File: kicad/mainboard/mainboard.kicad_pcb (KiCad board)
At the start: 2 copper layers, 190.5 x 66 mm, 146 parts, among them J1 +12V BATTERY, J10 Conn 1x4, J12 Conn 02x03, J13 Conn_02x12, J2 REMOTE INPUT, J3 RADIO INTERFACE, J4 MIC INPUT, J5 LINE INPUT, J6 OUTPUT A, J7 OUTPUT B, J8 VDC INPUT, J9 LINK INPUT, T1 IRL520N, T2 IRL520N, T3 IRF9Z24, T4 IRL520N, T5 IRL520N, T6 IRF9Z24, U1 ATMEGA16/32-P, U10 LM358N, U11 7809TV, U12 7809TV, U13 7805TV, U2 LM324N, U4 LM358N, U5 LM2941T, U7 LTC1661, U8 MAX548A, U9 MAX232

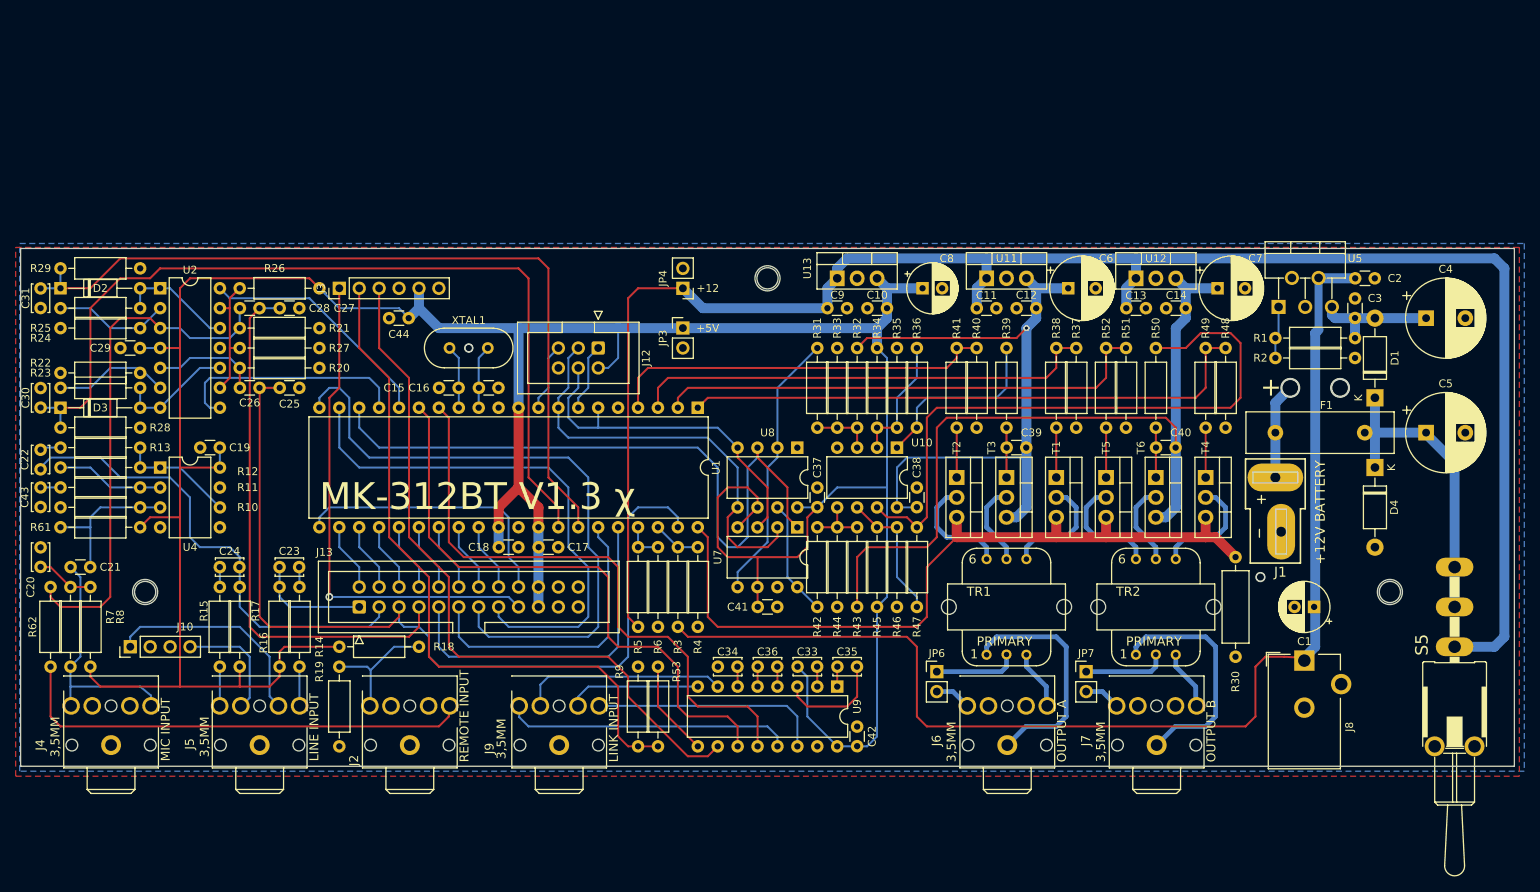
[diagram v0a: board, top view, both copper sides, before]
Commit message: Tiny fixups on mainboard: mounting holes and one audio jack
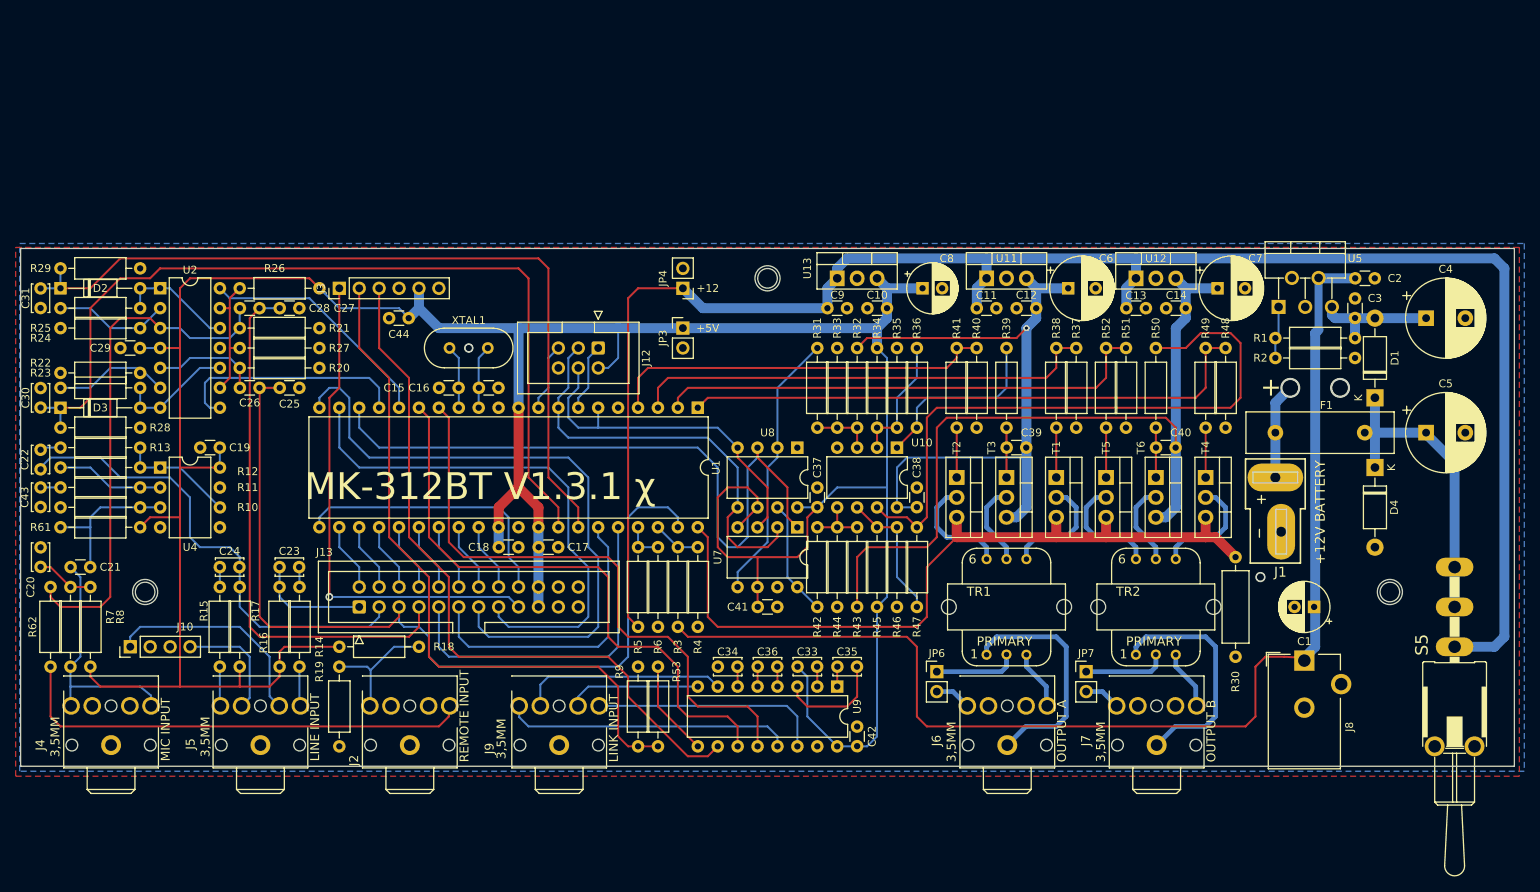
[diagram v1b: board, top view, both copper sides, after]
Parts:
- H1, H2, H3: footprint MountingHole:MountingHole_2.7mm_M2.5 -> MountingHole:MountingHole_2.5mm
- moved J5 0.10 mm to (81.3, 116.8)
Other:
- board text added: "MK-312BT V1.3.1 χ"
- board text removed: "MK-312BT V1.3 χ"
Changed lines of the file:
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@@
   )
   (paper "A4")
+  (title_block
+    (title "MK312-BT Mainboard")
+    (date "2022-08-01")
+    (rev "1.3.1-Chi")
+  )
   (layers
     (0 "F.Cu" signal)
@@
       (layerselection 0x00010fc_ffffffff)
       (disableapertmacros false)
-      (usegerberextensions false)
+      (usegerberextensions true)
       (usegerberattributes true)
       (usegerberadvancedattributes true)
-      (creategerberjobfile true)
+      (creategerberjobfile false)
       (svguseinch false)
       (svgprecision 6)
@@
       (outputformat 1)
       (mirror false)
-      (drillshape 1)
+      (drillshape 0)
       (scaleselection 1)
-      (outputdirectory "")
+      (outputdirectory "gerber")
     )
   )
@@
   )
   (footprint "mk312:STX3100" (layer "F.Cu")
-    (at 81.18 116.84 90)
+    (at 81.28 116.84 90)
     (descr "<b>MIC/HEADPHONE JACK</b><p>\nKS-S stereo microphone/headphone jack<p>\n PG203JN (Schukat)")
     (property "Sheetfile" "Input_stage.kicad_sch")
@@
     )
   )
-  (footprint "MountingHole:MountingHole_2.7mm_M2.5" (layer "F.Cu")
+  (footprint "MountingHole:MountingHole_2.5mm" (layer "F.Cu")
     (at 66.675 94.615)
-    (descr "Mounting Hole 2.7mm, no annular, M2.5")
-    (tags "mounting hole 2.7mm no annular m2.5")
+    (descr "Mounting Hole 2.5mm, no annular")
+    (tags "mounting hole 2.5mm no annular")
     (property "Sheetfile" "mainboard.kicad_sch")
     (property "Sheetname" "")
     (attr exclude_from_pos_files)
-    (fp_text reference "H3" (at 0 -3.7) (layer "F.SilkS") hide
+    (fp_text reference "H3" (at 0 -3.5) (layer "F.SilkS") hide
       (effects (font (size 1 1) (thickness 0.15)))
     )
-    (fp_text value "MountingHole" (at 0 3.7) (layer "F.Fab")
+    (fp_text value "MountingHole" (at 0 3.5) (layer "F.Fab")
       (effects (font (size 1 1) (thickness 0.15)))
     )
@@
       (effects (font (size 1 1) (thickness 0.15)))
     )
-    (fp_circle (center 0 0) (end 2.7 0) (layer "Cmts.User") (width 0.15) (fill none))
-    (fp_circle (center 0 0) (end 2.95 0) (layer "F.CrtYd") (width 0.05) (fill none))
-    (pad "" np_thru_hole circle (at 0 0) (size 2.7 2.7) (drill 2.7) (layers *.Cu *.Mask))
+    (fp_circle (center 0 0) (end 2.5 0) (layer "Cmts.User") (width 0.15) (fill none))
+    (fp_circle (center 0 0) (end 2.75 0) (layer "F.CrtYd") (width 0.05) (fill none))
+    (pad "" np_thru_hole circle (at 0 0) (size 2.5 2.5) (drill 2.5) (layers *.Cu *.Mask))
   )
   (footprint "Resistor_THT:R_Axial_DIN0207_L6.3mm_D2.5mm_P10.16mm_Horizontal" (layer "F.Cu")
@@
     (fp_line (start 4.52 8.99) (end -1.98 8.99) (layer "F.Fab") (width 0.1))
     (fp_line (start 5.72 -5.1) (end 5.72 10.18) (layer "F.Fab") (width 0.1))
-    (pad "1" thru_hole roundrect (at 0 0 270) (size 1.7 1.7) (drill 1) (layers *.Cu *.Mask) (roundrect_rratio 0.147059)
+    (pad "1" thru_hole roundrect (at 0 0 270) (size 1.7 1.7) (drill 1) (layers *.Cu *.Mask) (roundrect_rratio 0.1470588235)
       (net 76 "/CPU & link/MISO") (pinfunction "Pin_1") (pintype "passive"))
     (pad "2" thru_hole circle (at 2.54 0 270) (size 1.7 1.7) (drill 1) (layers *.Cu *.Mask)
@@
       (net 106 "Net-(J9-Pad5)") (pinfunction "5") (pintype "passive") (solder_mask_margin 0.1016))
   )
-  (footprint "MountingHole:MountingHole_2.7mm_M2.5" (layer "F.Cu")
+  (footprint "MountingHole:MountingHole_2.5mm" (layer "F.Cu")
     (at 146.05 54.61)
-    (descr "Mounting Hole 2.7mm, no annular, M2.5")
-    (tags "mounting hole 2.7mm no annular m2.5")
+    (descr "Mounting Hole 2.5mm, no annular")
+    (tags "mounting hole 2.5mm no annular")
     (property "Sheetfile" "mainboard.kicad_sch")
     (property "Sheetname" "")
     (attr exclude_from_pos_files)
-    (fp_text reference "H2" (at 0 -3.7) (layer "F.SilkS") hide
+    (fp_text reference "H2" (at 0 -3.5) (layer "F.SilkS") hide
       (effects (font (size 1 1) (thickness 0.15)))
     )
-    (fp_text value "MountingHole" (at 0 3.7) (layer "F.Fab")
+    (fp_text value "MountingHole" (at 0 3.5) (layer "F.Fab")
       (effects (font (size 1 1) (thickness 0.15)))
     )
@@
       (effects (font (size 1 1) (thickness 0.15)))
     )
-    (fp_circle (center 0 0) (end 2.7 0) (layer "Cmts.User") (width 0.15) (fill none))
-    (fp_circle (center 0 0) (end 2.95 0) (layer "F.CrtYd") (width 0.05) (fill none))
-    (pad "" np_thru_hole circle (at 0 0) (size 2.7 2.7) (drill 2.7) (layers *.Cu *.Mask))
+    (fp_circle (center 0 0) (end 2.5 0) (layer "Cmts.User") (width 0.15) (fill none))
+    (fp_circle (center 0 0) (end 2.75 0) (layer "F.CrtYd") (width 0.05) (fill none))
+    (pad "" np_thru_hole circle (at 0 0) (size 2.5 2.5) (drill 2.5) (layers *.Cu *.Mask))
   )
   (footprint "Capacitor_THT:C_Disc_D3.4mm_W2.1mm_P2.50mm" (layer "F.Cu")
@@
     (fp_line (start -2.18 -5.1) (end 5.72 -5.1) (layer "F.Fab") (width 0.1))
     (fp_line (start 4.52 31.85) (end -1.98 31.85) (layer "F.Fab") (width 0.1))
-    (pad "1" thru_hole roundrect (at 0 0 90) (size 1.7 1.7) (drill 1) (layers *.Cu *.Mask) (roundrect_rratio 0.147059)
+    (pad "1" thru_hole roundrect (at 0 0 90) (size 1.7 1.7) (drill 1) (layers *.Cu *.Mask) (roundrect_rratio 0.1470588235)
       (net 19 "RB10") (pinfunction "Pin_1") (pintype "passive"))
     (pad "2" thru_hole circle (at 2.54 0 90) (size 1.7 1.7) (drill 1) (layers *.Cu *.Mask)
@@
     )
   )
-  (footprint "MountingHole:MountingHole_2.7mm_M2.5" (layer "F.Cu")
+  (footprint "MountingHole:MountingHole_2.5mm" (layer "F.Cu")
     (at 225.425 94.615)
-    (descr "Mounting Hole 2.7mm, no annular, M2.5")
-    (tags "mounting hole 2.7mm no annular m2.5")
+    (descr "Mounting Hole 2.5mm, no annular")
+    (tags "mounting hole 2.5mm no annular")
     (property "Sheetfile" "mainboard.kicad_sch")
     (property "Sheetname" "")
     (attr exclude_from_pos_files)
-    (fp_text reference "H1" (at 0 -3.7) (layer "F.SilkS") hide
+    (fp_text reference "H1" (at 0 -3.5) (layer "F.SilkS") hide
       (effects (font (size 1 1) (thickness 0.15)))
     )
-    (fp_text value "MountingHole" (at 0 3.7) (layer "F.Fab")
+    (fp_text value "MountingHole" (at 0 3.5) (layer "F.Fab")
       (effects (font (size 1 1) (thickness 0.15)))
     )
@@
       (effects (font (size 1 1) (thickness 0.15)))
     )
-    (fp_circle (center 0 0) (end 2.7 0) (layer "Cmts.User") (width 0.15) (fill none))
-    (fp_circle (center 0 0) (end 2.95 0) (layer "F.CrtYd") (width 0.05) (fill none))
-    (pad "" np_thru_hole circle (at 0 0) (size 2.7 2.7) (drill 2.7) (layers *.Cu *.Mask))
+    (fp_circle (center 0 0) (end 2.5 0) (layer "Cmts.User") (width 0.15) (fill none))
+    (fp_circle (center 0 0) (end 2.75 0) (layer "F.CrtYd") (width 0.05) (fill none))
+    (pad "" np_thru_hole circle (at 0 0) (size 2.5 2.5) (drill 2.5) (layers *.Cu *.Mask))
   )
   (footprint "Package_TO_SOT_THT:TO-220-3_Vertical" (layer "F.Cu")
@@
     (effects (font (size 2.3368 2.3368) (thickness 0.2032)) (justify left bottom))
   )
-  (gr_text "MK-312BT V1.3 χ" (at 88.9 84.455) (layer "F.SilkS")
+  (gr_text "MK-312BT V1.3.1 χ" (at 86.995 83.185) (layer "F.SilkS")
     (effects (font (size 3.429 3.429) (thickness 0.381)) (justify left bottom))
   )

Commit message: Bringing mainboard up to par with V1.4 schematics based on images. Rerouted a few lines since they could not pass below the MOSFETs due to a different footprint/pad size.
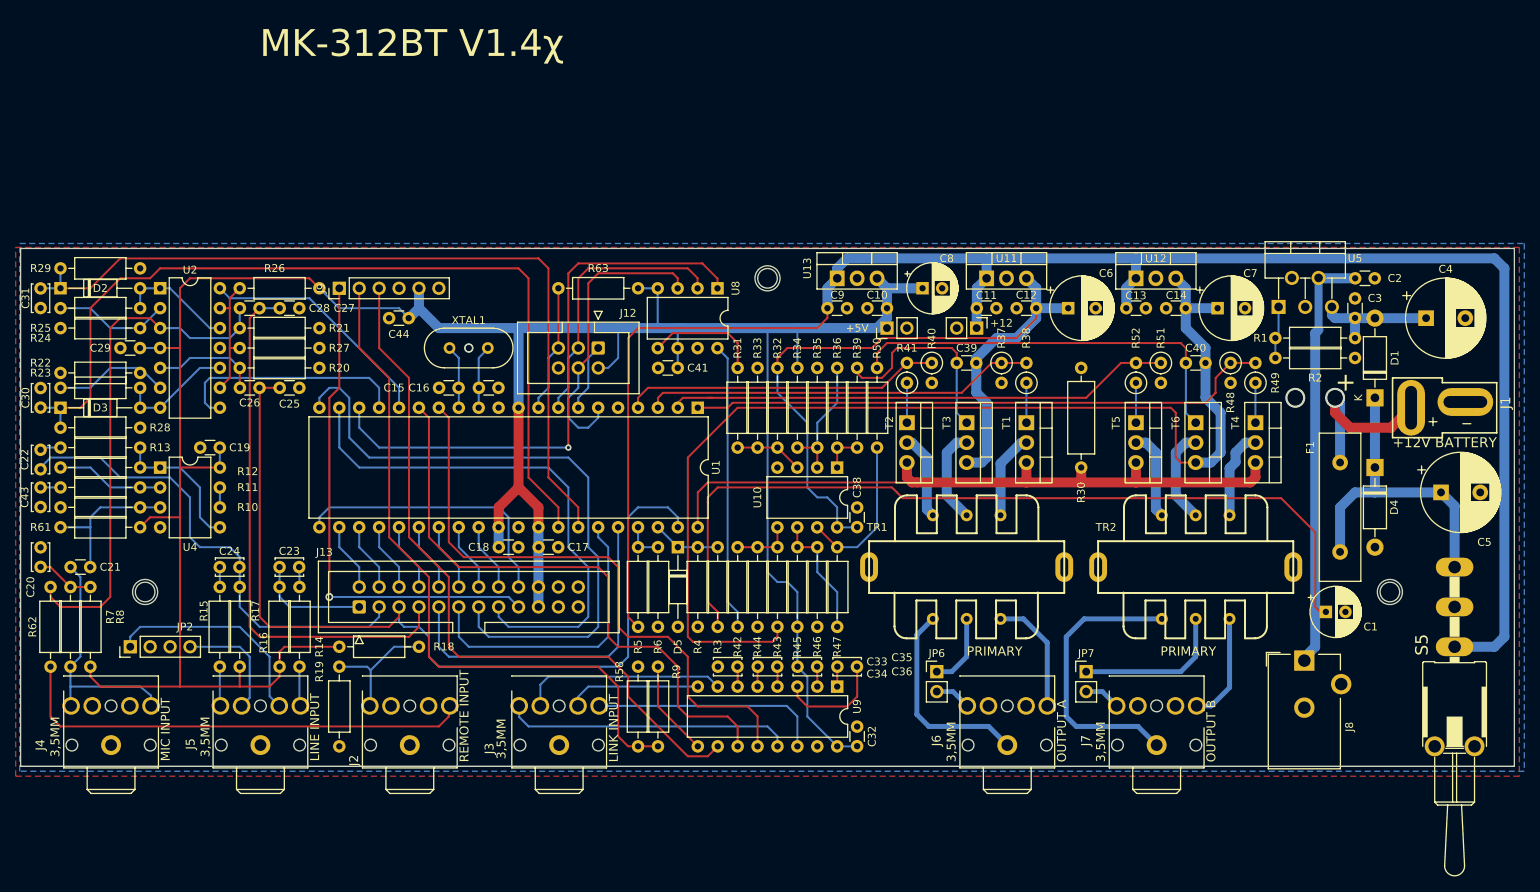
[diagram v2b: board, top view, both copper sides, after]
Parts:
- removed C37: 0.1uF, Capacitor_THT:C_Disc_D3.0mm_W1.6mm_P2.50mm
- removed U7: LTC1661, Package_DIP:DIP-8_W7.62mm
- added D5: 1N4148, Diode_THT:D_DO-35_SOD27_P10.16mm_Horizontal, F.Cu at (134.6, 88.9)
- added R63: 10k, Resistor_THT:R_Axial_DIN0207_L6.3mm_D2.5mm_P10.16mm_Horizontal, F.Cu at (129.5, 55.9)
- R30: value 0.5R -> 0.27R
- R37, R38, R40, R41, R48, R49, R51, R52: footprint Resistor_THT:R_Axial_DIN0207_L6.3mm_D2.5mm_P10.16mm_Horizontal -> Resistor_THT:R_Axial_DIN0207_L6.3mm_D2.5mm_P2.54mm_Vertical
- TR1, TR2: value 42TL004 -> 42TU200; footprint mk312:42TL -> mk312:Transformer_Xicon_42TU
- U8: value MAX548A -> LTC1661
- moved JP4 37.8 mm to (172.7, 61.0), turned to -90 degrees
- moved R50 36.4 mm to (160.0, 66.0), turned to -90 degrees
- moved C41 32.1 mm to (134.6, 66.0), turned to 180 degrees
- moved JP3 26.0 mm to (161.3, 61.0), turned to 90 degrees
- moved R30 22.8 mm to (186.1, 78.7), turned to 90 degrees
- moved U8 22.7 mm to (139.7, 55.9)
- moved R39 20.5 mm to (157.5, 66.0), turned to -90 degrees
- moved J1 19.5 mm to (228.1, 71.1), turned to 90 degrees
- moved C39 12.5 mm to (170.2, 65.4)
- moved C40 11.4 mm to (199.4, 65.4)
- moved R31 10.5 mm to (142.2, 76.2)
- moved R32 10.5 mm to (147.3, 66.0)
- moved R33 10.5 mm to (144.8, 76.2)
- moved R34 10.5 mm to (149.9, 66.0)
- moved R35 10.5 mm to (152.4, 76.2)
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- renumbered C42 to C32, J9 to J3, J3 to J9, J10 to JP2, R9 to R58, R53 to R9
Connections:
- U4 pad 5: GND -> Net-(R12-Pad1)
- U4 pad 6: Net-(R12-Pad1) -> Net-(U4-Pad6)
- U4 pad 7: unconnected-(U4-Pad7) -> Net-(U4-Pad6)
- U8 pad 1: GND -> ~{CS}
- U8 pad 2: Net-(R31-Pad2) -> PB7
- U8 pad 3: ~{CS} -> PB5
- U8 pad 4: PB5 -> +5V
- U8 pad 5: PB7 -> Net-(R31-Pad2)
- U8 pad 7: Net-(R42-Pad2) -> GND
- U8 pad 8: +5V -> Net-(R42-Pad2)
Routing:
- net Net-(R47-Pad1): track 80.8 -> 19.9 mm
- net +5V: track 394.2 -> 347.0 mm
- net Net-(C40-Pad1): track 6.35 -> 52.1 mm
- net 9V2: track 103.0 -> 142.1 mm
- net Net-(R42-Pad2): track 14.8 -> 36.6 mm
- net Net-(R31-Pad2): track 34.7 -> 14.7 mm
- net Net-(C39-Pad1): track 6.35 -> 26.0 mm
- net PB7: track 54.3 -> 35.1 mm
- net Net-(R36-Pad2): track 23.7 -> 5.09 mm
- net 9V1: track 84.7 -> 99.9 mm, vias 1 -> 0
- net ~{CS}: track 88.3 -> 74.1 mm, vias 0 -> 1
- net +VDC: track 151.5 -> 163.4 mm
- net PA0: track 99.5 -> 88.7 mm
- net Net-(F1-Pad1): track 12.2 -> 22.0 mm
- net PB2: track 59.5 -> 50.1 mm
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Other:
- board text added: "MK-312BT V1.4χ"
- board text removed: "MK-312BT V1.3.1 χ"

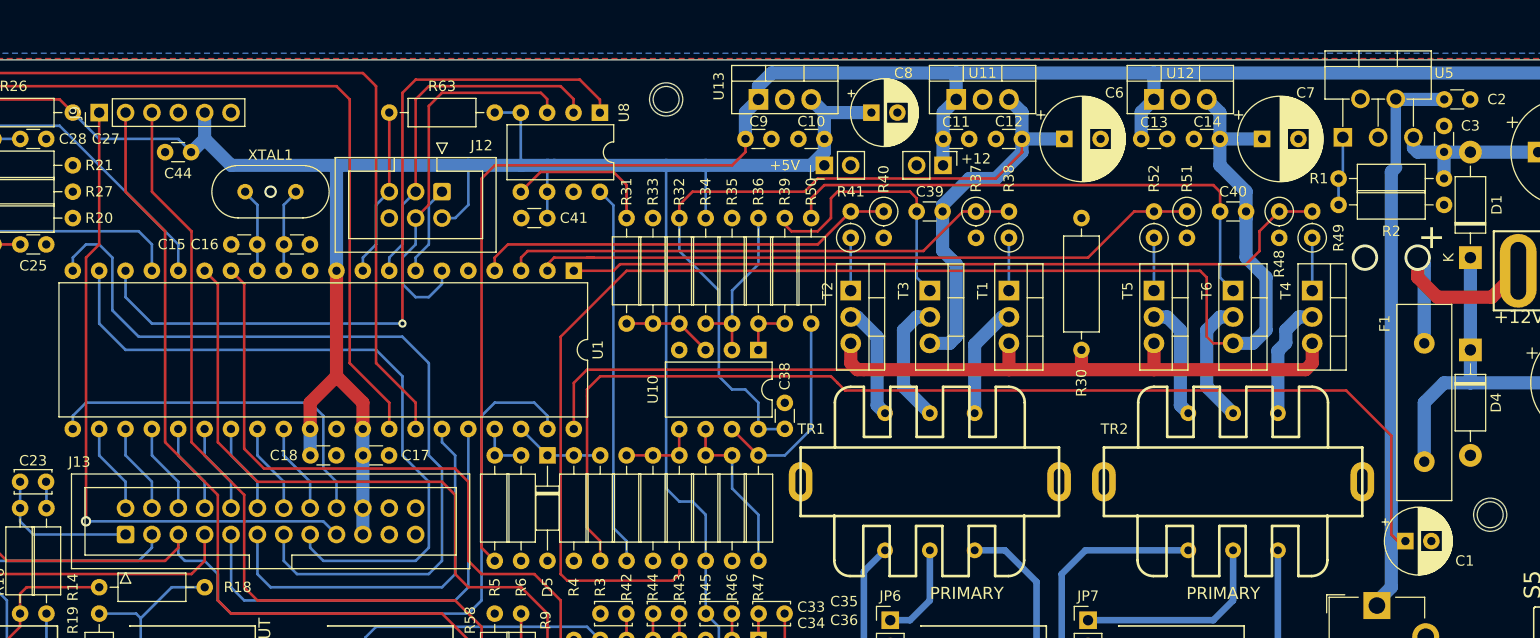
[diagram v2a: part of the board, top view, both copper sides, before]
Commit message: Brought component numbers back in line with the original schematics
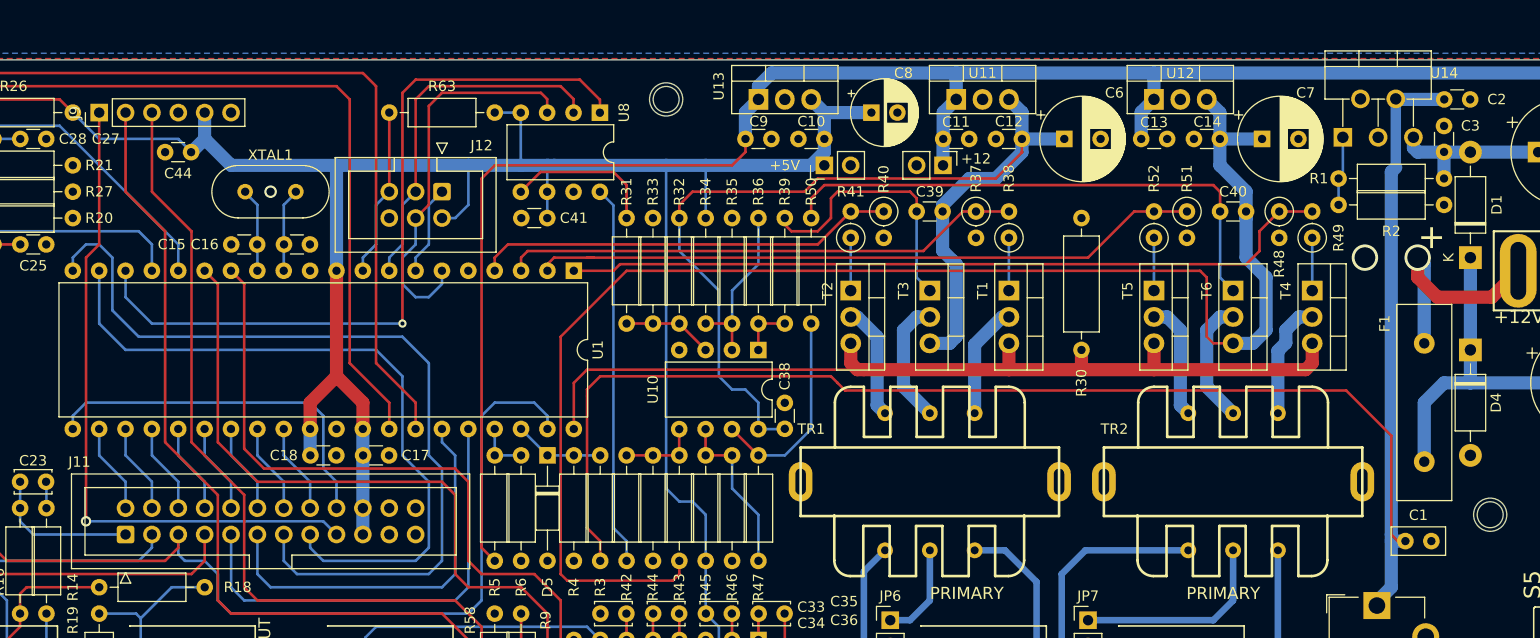
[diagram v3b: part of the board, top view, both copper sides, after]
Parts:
- C1: value 10uF -> 10uF ceramic; footprint Capacitor_THT:CP_Radial_D6.3mm_P2.50mm -> Capacitor_THT:C_Disc_D5.0mm_W2.5mm_P2.50mm
- R28, R42: value 100K -> 100k
- renumbered J13 to J11, U5 to U14
